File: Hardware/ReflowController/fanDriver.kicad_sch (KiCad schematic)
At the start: 8 parts, among them U3 TB67H400AFNG

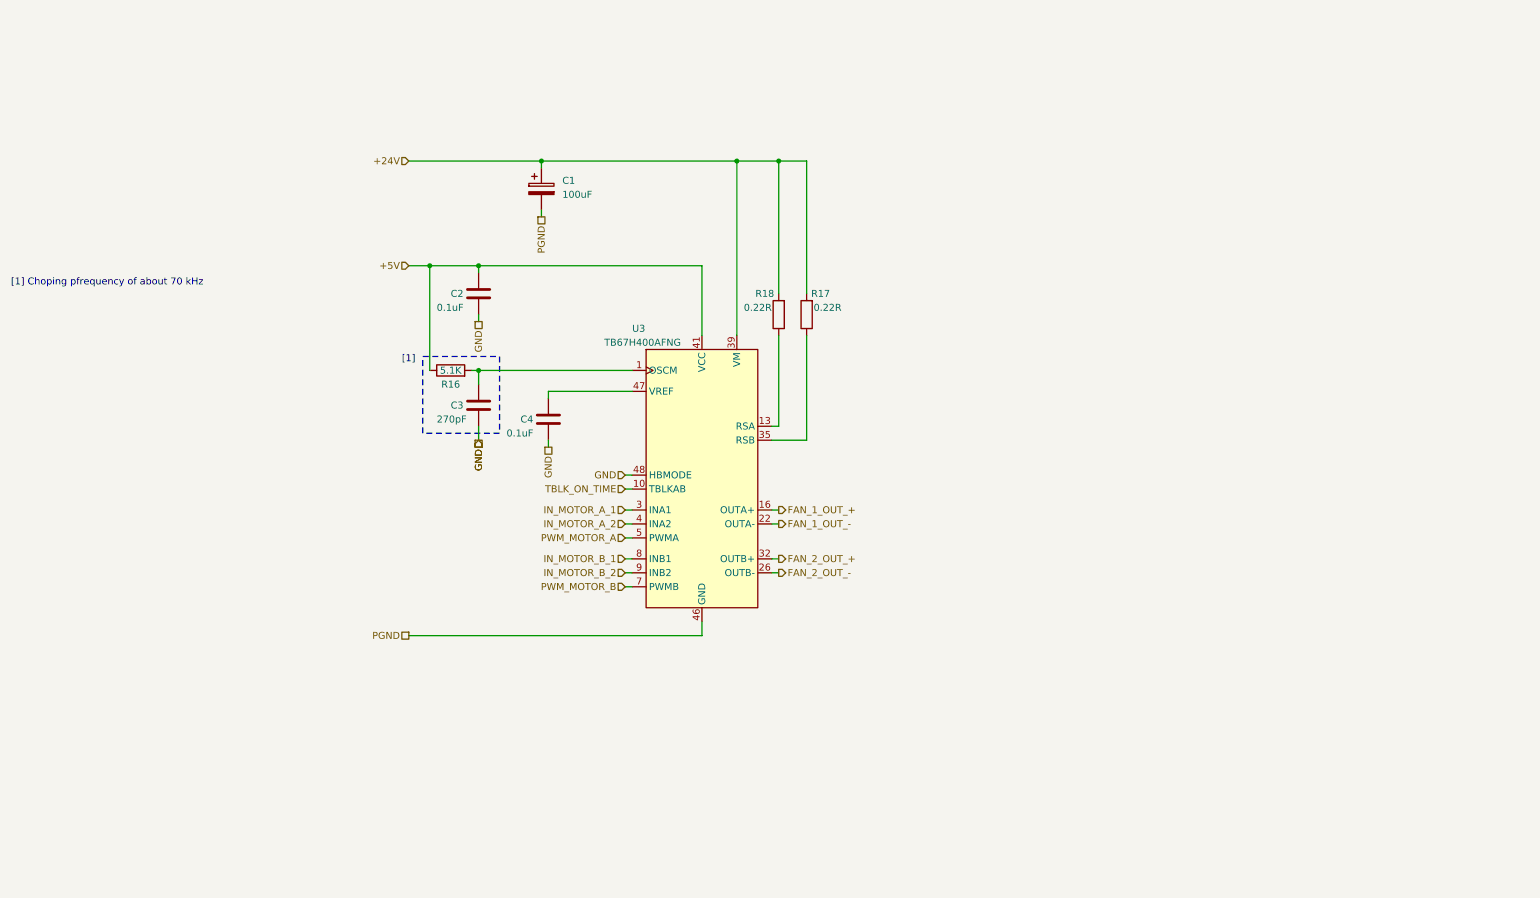
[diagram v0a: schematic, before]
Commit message: Finished the fan controllers calculations, added the wago connectors, added notes
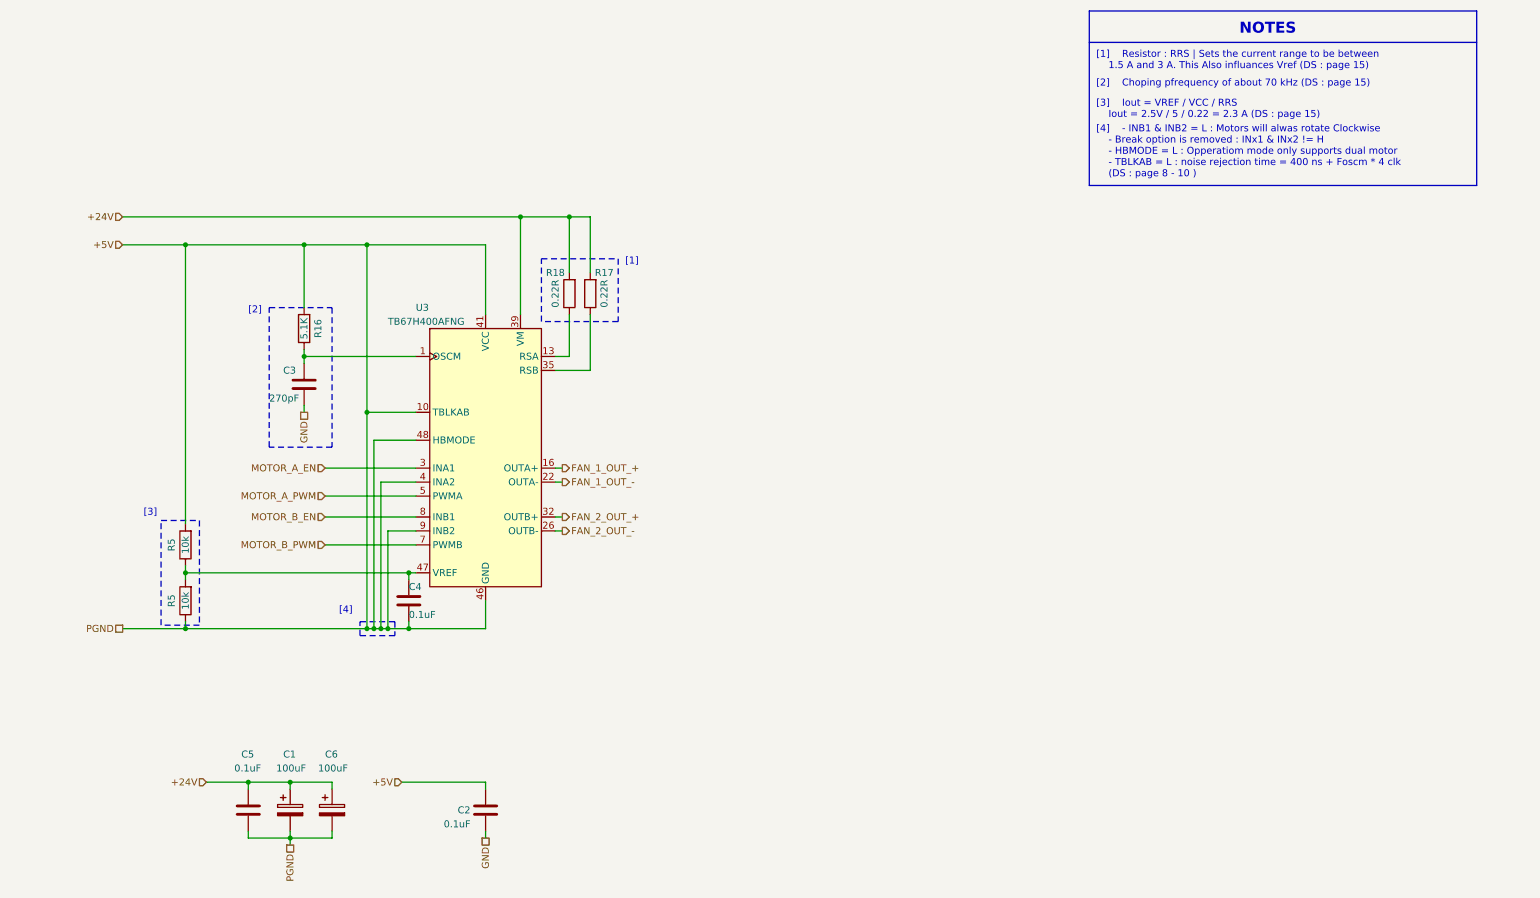
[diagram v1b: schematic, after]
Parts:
- added C5: 0.1uF, Capacitor_SMD:C_0603_1608Metric_Pad1.08x0.95mm_HandSolder, symbol Device:C
- added C6: 100uF, Capacitor_SMD:CP_Elec_8x10.5, symbol Device:C_Polarized
- added R5 (x2): 10k, Resistor_SMD:R_0603_1608Metric_Pad0.98x0.95mm_HandSolder, symbol Device:R
- C1: footprint (none) -> Capacitor_SMD:CP_Elec_8x10.5; disti_no (none) -> PCE3809TR-ND; man (none) -> panasonic; man_no (none) -> EEE-FK1H101P
- C2, C4: footprint (none) -> Capacitor_SMD:C_0603_1608Metric_Pad1.08x0.95mm_HandSolder; disti digieky -> digikey; disti_no (none) -> 1276-1935-2-ND; man (none) -> samsung; man_no (none) -> CL10B104KB8NNWC
- C3: footprint (none) -> Capacitor_SMD:C_0603_1608Metric_Pad1.08x0.95mm_HandSolder; disti digieky -> digikey; disti_no (none) -> 1276-7006-2-ND; man (none) -> samsung; man_no (none) -> CL10C271JB81PNC
- R16: footprint (none) -> Resistor_SMD:R_0603_1608Metric_Pad0.98x0.95mm_HandSolder; disti (none) -> digikey; disti_no (none) -> 311-5.10KHRTR-ND; man (none) -> yageo; man_no (none) -> RC0603FR-075K1L
- R17, R18: footprint (none) -> Resistor_SMD:R_0603_1608Metric_Pad0.98x0.95mm_HandSolder; disit (none) -> digikey; disti_no (none) -> P.22AJTR-ND; man (none) -> panasonic; man_no (none) -> ERJ-3RQFR22V
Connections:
- net IN_MOTOR_A_2 is gone; now on net +5V: U3.4 (INA2)
- net IN_MOTOR_B_2 is gone; now on net +5V: U3.9 (INB2)
- net PGND is gone; now on net +5V: C1.2, U3.11 (GND), U3.20 (GND), U3.24 (GND), U3.25 (GND), U3.29 (GND), U3.46 (GND)
- net TBLK_ON_TIME is gone; now on net +5V: U3.10 (TBLKAB)
- net +24V: now also C5.1, C6.1
- net +5V: now also C4.2, R16.2, U3.48 (HBMODE), C5.2, C6.2, R5.1, R5.2; no longer R16.1
- net GND: no longer C4.2, U3.48 (HBMODE)
- net at C3.1, U3.1 (OSCM): now also R16.1; no longer R16.2
- net at C4.1, U3.47 (VREF): now also R5.1, R5.2
- net IN_MOTOR_A_1 renamed MOTOR_A_EN
- net IN_MOTOR_B_1 renamed MOTOR_B_EN
- net PWM_MOTOR_A renamed MOTOR_A_PWM
- net PWM_MOTOR_B renamed MOTOR_B_PWM
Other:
- note added: "NOTES"
- note added: "[1] Resistor : RRS | Sets the current range to be between 1.5 A and 3 A. This Also influances Vref (DS : page 15)"
- note added: "[2]"
- note added: "[2] Choping pfrequency of about 70 kHz (DS : page 15)"
- note added: "[3]"
- note added: "[3] Iout = VREF / VCC / RRS Iout = 2.5V / 5 / 0.22 = 2.3 A (DS : page 15)"
- note added: "[4]"
- note added: "[4] - INB1 & INB2 = L : Motors will alwas rotate Clockwise - Break option is removed : INx1 & INx2 != H - HBMODE = L : Opperatiom mode only supports dual motor - TBLKAB = L : noise rejection time = 400 ns + Foscm * 4 clk (DS : page 8 - 10 )"
- note removed: "[1] Choping pfrequency of about 70 kHz"
- title: (none) -> Reflow Oven Control
- moved on the sheet: C1, C2, C3, R16, R18, U3

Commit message: added the schematic of the updated pwerAndUi branch(with uC schematic update
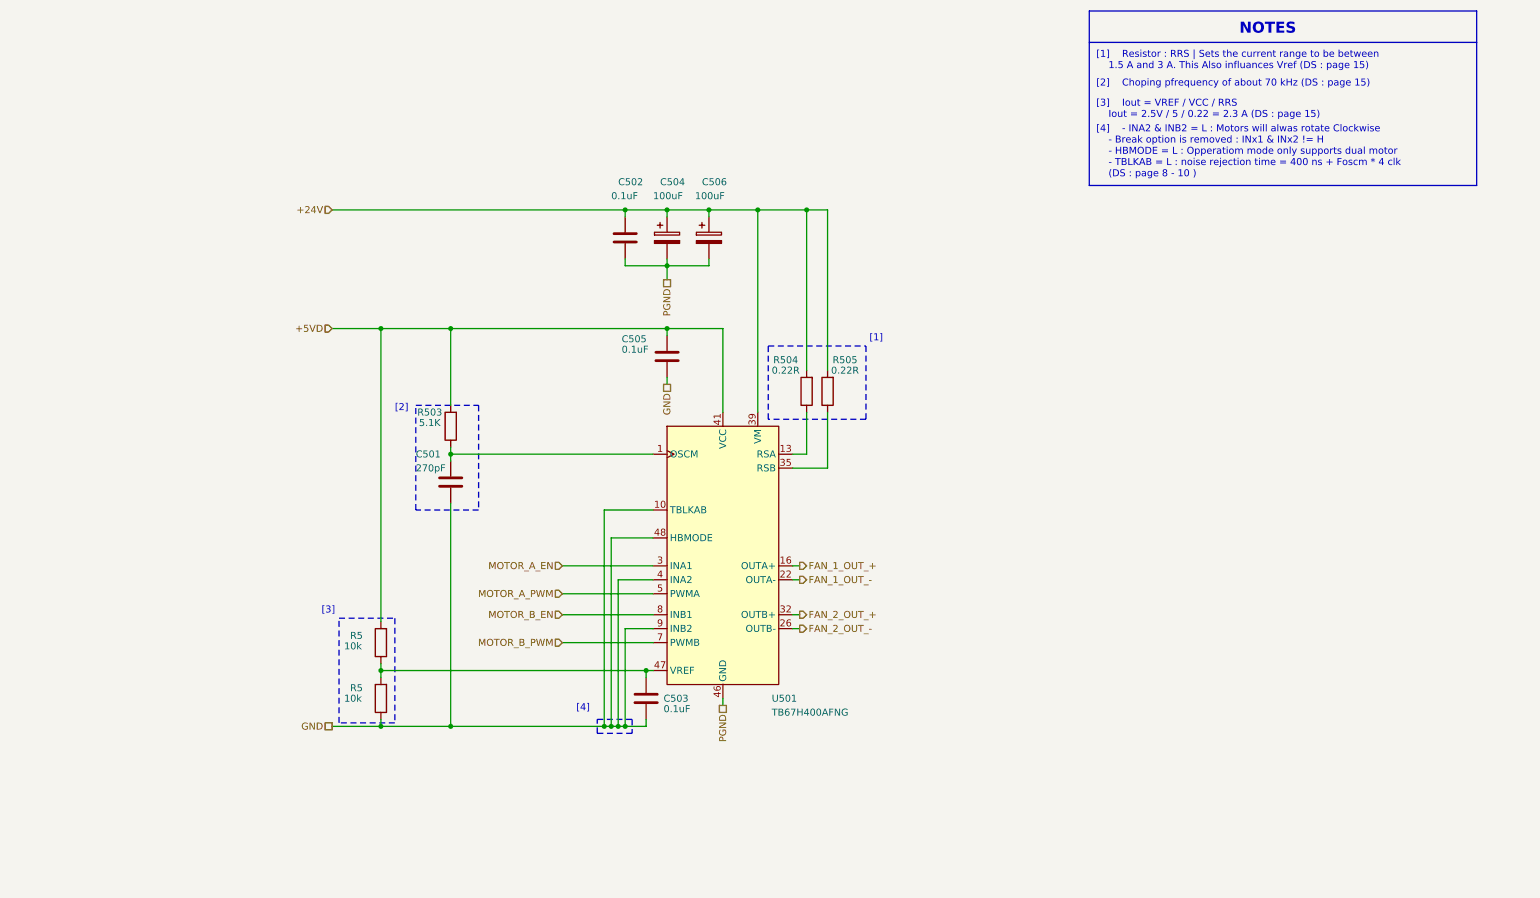
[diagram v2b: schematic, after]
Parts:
- renumbered C3 to C501, C5 to C502, C4 to C503, C1 to C504, C2 to C505, C6 to C506, R16 to R503, R18 to R504, R17 to R505, U3 to U501
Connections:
- net GND: now also C503.2, R5.1, U501.10 (TBLKAB), U501.4 (INA2), U501.48 (HBMODE), U501.9 (INB2)
- removed net +5V: C502.2, C503.2, C504.2, C505.1, C506.2, R5.1, R5.2, R503.2, U501.10 (TBLKAB), U501.11 (GND), U501.20 (GND), U501.24 (GND), U501.25 (GND), U501.29 (GND), U501.4 (INA2), U501.41 (VCC), U501.46 (GND), U501.48 (HBMODE), U501.9 (INB2)
- new net +5VD: C505.1, R5.2, R503.2, U501.41 (VCC)
- new net PGND: C502.2, C504.2, C506.2, U501.11 (GND), U501.20 (GND), U501.24 (GND), U501.25 (GND), U501.29 (GND), U501.46 (GND), U501.PAD (GND)
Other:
- note added: "[4] - INA2 & INB2 = L : Motors will alwas rotate Clockwise - Break option is removed : INx1 & INx2 != H - HBMODE = L : Opperatiom mode only supports dual motor - TBLKAB = L : noise rejection time = 400 ns + Foscm * 4 clk (DS : page 8 - 10 )"
- note removed: "[4] - INB1 & INB2 = L : Motors will alwas rotate Clockwise - Break option is removed : INx1 & INx2 != H - HBMODE = L : Opperatiom mode only supports dual motor - TBLKAB = L : noise rejection time = 400 ns + Foscm * 4 clk (DS : page 8 - 10 )"
- moved on the sheet: C501, C502, C503, C504, C505, C506, R5, R503, R504, R505, U501

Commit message: work on BOM cleanup
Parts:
- R504, R505: disit digikey -> (none); disti (none) -> digikey
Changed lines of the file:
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@@
       (effects (font (size 1.27 1.27)) hide)
     )
-    (property "disit" "digikey" (at 162.56 81.28 0)
+    (property "disit" "" (at 162.56 81.28 0)
       (effects (font (size 1.27 1.27)) hide)
     )
     (property "disti_no" "P.22AJTR-ND" (at 162.56 81.28 0)
+      (effects (font (size 1.27 1.27)) hide)
+    )
+    (property "disti" "digikey" (at 162.56 81.28 0)
       (effects (font (size 1.27 1.27)) hide)
     )
@@
       (effects (font (size 1.27 1.27)) hide)
     )
-    (property "disit" "digikey" (at 166.37 81.28 0)
+    (property "disit" "" (at 166.37 81.28 0)
       (effects (font (size 1.27 1.27)) hide)
     )
@@
       (effects (font (size 1.27 1.27)) hide)
     )
+    (property "disti" "digikey" (at 166.37 81.28 0)
+      (effects (font (size 1.27 1.27)) hide)
+    )
